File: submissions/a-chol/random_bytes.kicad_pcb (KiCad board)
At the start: 2 copper layers, 76.6 x 33 mm, 36 parts, among them Q1 MMBT3904, Q2 2N3904, Q3 MMBT3904, SW1 SW_DIP_x04, U1 ATmega32U4-AU, U2 TPS61041DBV, Y1 16MHz

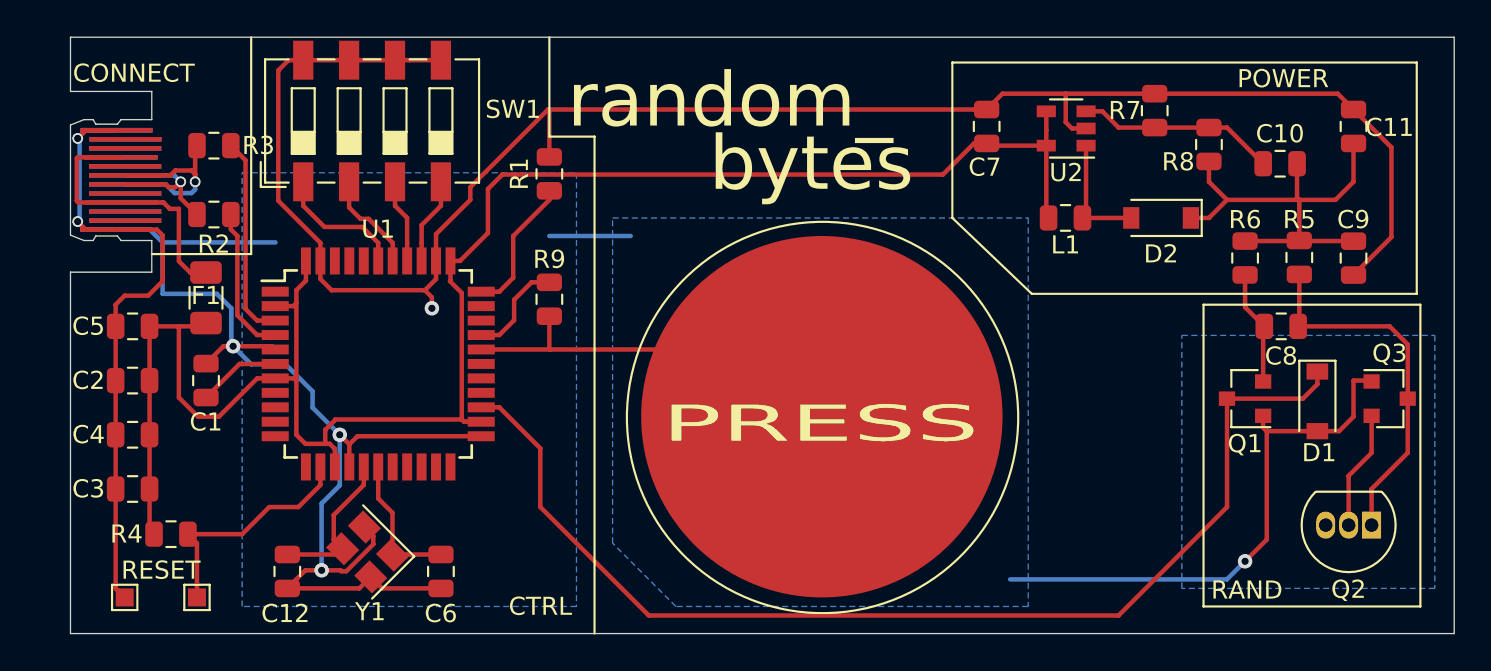
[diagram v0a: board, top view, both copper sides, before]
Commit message: a-chol: fix usb-c connector connections and add some artworks.
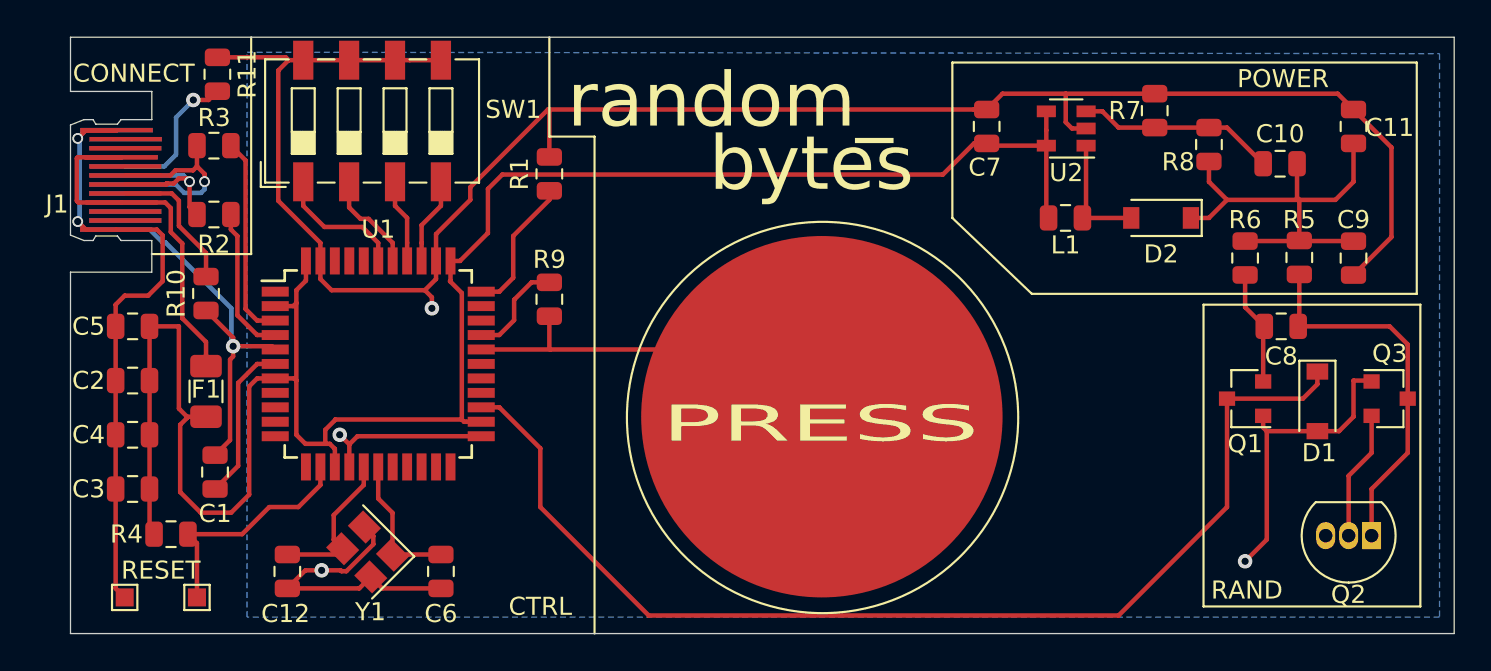
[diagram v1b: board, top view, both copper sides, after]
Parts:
- added R10: 5.1k, Resistor_SMD:R_0805_2012Metric, F.Cu at (97.5, 84.2)
- added R11: 5.1k, Resistor_SMD:R_0805_2012Metric, F.Cu at (98.1, 72.0)
- CapSensor1, GND_Pad1, J1, RST_Pad1: renamed from  
- moved F1 5.18 mm to (97.5, 89.6)
- moved C1 5.09 mm to (98.0, 94.1)
- moved Q2 0.58 mm to (162.0, 97.6)
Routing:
- net GND: track 241.2 -> 211.1 mm
- net +5V: track 103.0 -> 113.7 mm
- net Net-(J1-PadA5): track 0.00 -> 7.96 mm
- net Net-(J1-PadB5): track 0.00 -> 7.90 mm, vias 0 -> 1
- net VCC: track 17.4 -> 21.8 mm
- net Net-(C1-Pad1): track 4.60 -> 8.89 mm
- net D+: track 8.66 -> 9.56 mm
